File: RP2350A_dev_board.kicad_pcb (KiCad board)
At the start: 2 copper layers, 50 x 60 mm, 52 parts, among them J1 Debug Headers, J2 USB_C_Female_USB2.0_16P, J3 I2C Headers, SW1 Button, SW2 Bootstrap, U1 USBLC6-2SC6, U2 SPX3819M5-L-3-3, U3 RP2350A, U4 W25Q128JVS, Y2 12MHz Crystal GND2,4

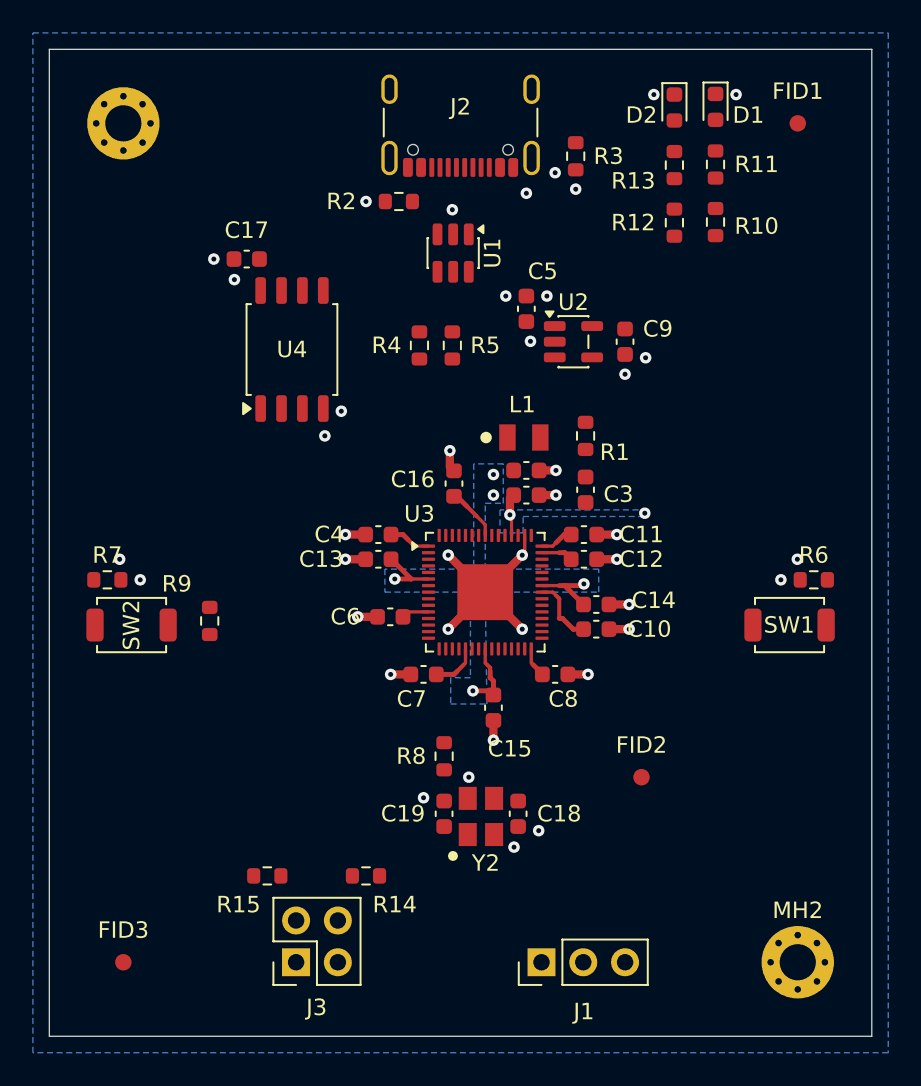
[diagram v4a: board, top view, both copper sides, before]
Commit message: Replaced +1V1 and +3V3 planes with wide routes. Routed all power. Finished all routing.
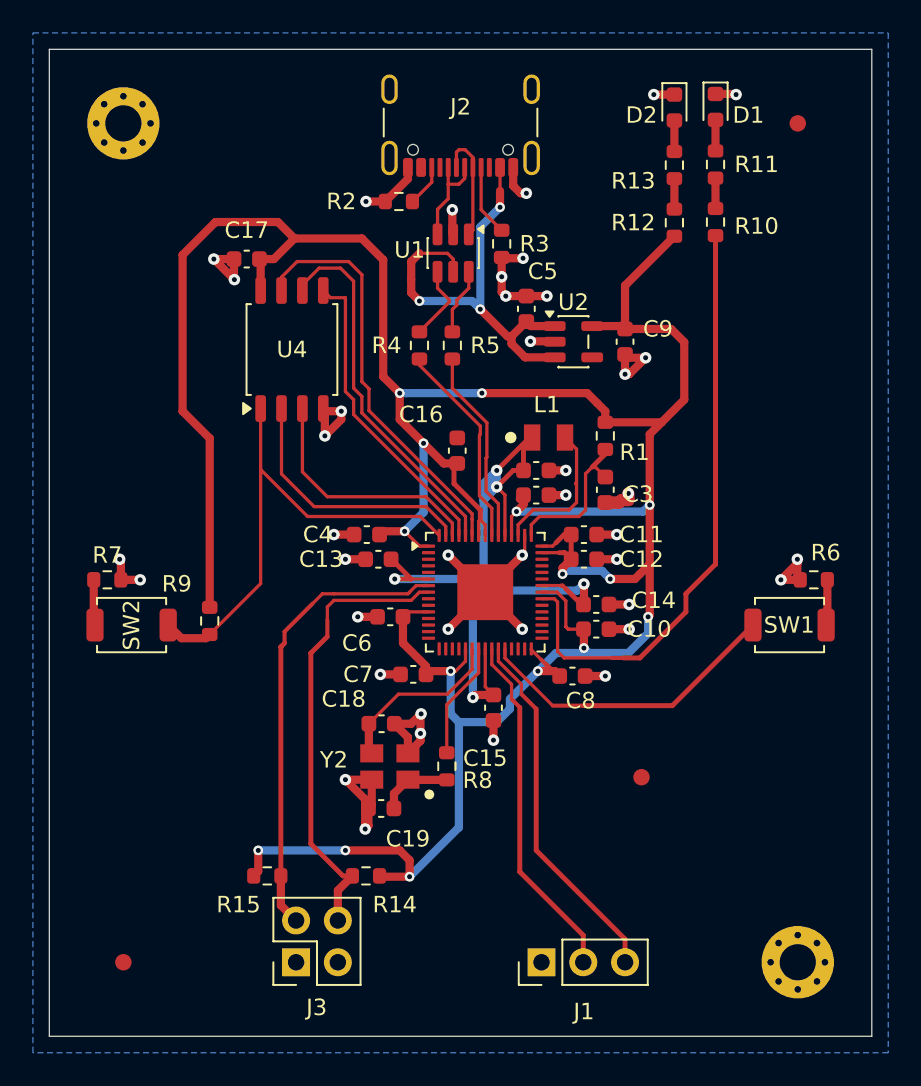
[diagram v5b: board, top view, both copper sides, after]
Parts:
- moved C18 9.94 mm to (143.2, 112.0), turned to 180 degrees
- moved R3 6.97 mm to (150.5, 82.8)
- moved Y2 4.99 mm to (145.5, 115.4), turned to 180 degrees
- moved C19 3.84 mm to (143.2, 117.2), turned to 0 degrees
- moved C16 2.01 mm to (147.8, 95.4)
- moved L1 1.50 mm to (154.3, 94.6)
- moved C3 1.20 mm to (156.8, 97.8)
- moved R1 1.20 mm to (156.8, 94.5)
- moved C8 1.05 mm to (154.8, 109.1)
- moved C4 0.70 mm to (142.3, 100.5)
- moved R8 0.63 mm to (147.2, 114.6)
- moved C7 0.62 mm to (145.1, 109.0)
- moved C1 0.60 mm to (152.6, 98.1)
- moved C2 0.60 mm to (152.6, 96.6)
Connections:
- net /USB_DM renamed /USB_DN
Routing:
- net +3V3: track 23.0 -> 204.5 mm, vias 2 -> 15
- net GND: track 29.6 -> 82.7 mm
- net +1V1: track 12.4 -> 52.8 mm
- net /GPIO25: track 0.00 -> 36.8 mm
- net /QSPI_SS: track 0.00 -> 30.5 mm
- net +VBUS: track 0.00 -> 28.4 mm, vias 0 -> 3
- net /I2C0_SDA: track 0.00 -> 27.9 mm
- net /I2C0_SCL: track 0.00 -> 27.7 mm
- net /QSPI_SD3: track 0.00 -> 25.0 mm
- net /QSPI_SCLK: track 0.00 -> 22.5 mm
- net /SWDIO: track 0.00 -> 22.2 mm
- net /SWCLK: track 0.00 -> 21.4 mm
- net Net-(U3-RUN): track 0.00 -> 18.9 mm
- net /QSPI_SD0: track 0.00 -> 18.8 mm
- net /QSPI_SD1: track 0.00 -> 15.8 mm
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- removed copper zone on B.Cu, net +1V1
- removed copper zone on B.Cu, net +3V3

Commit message: Finished routing. Cleared ERC on schematic and layout.
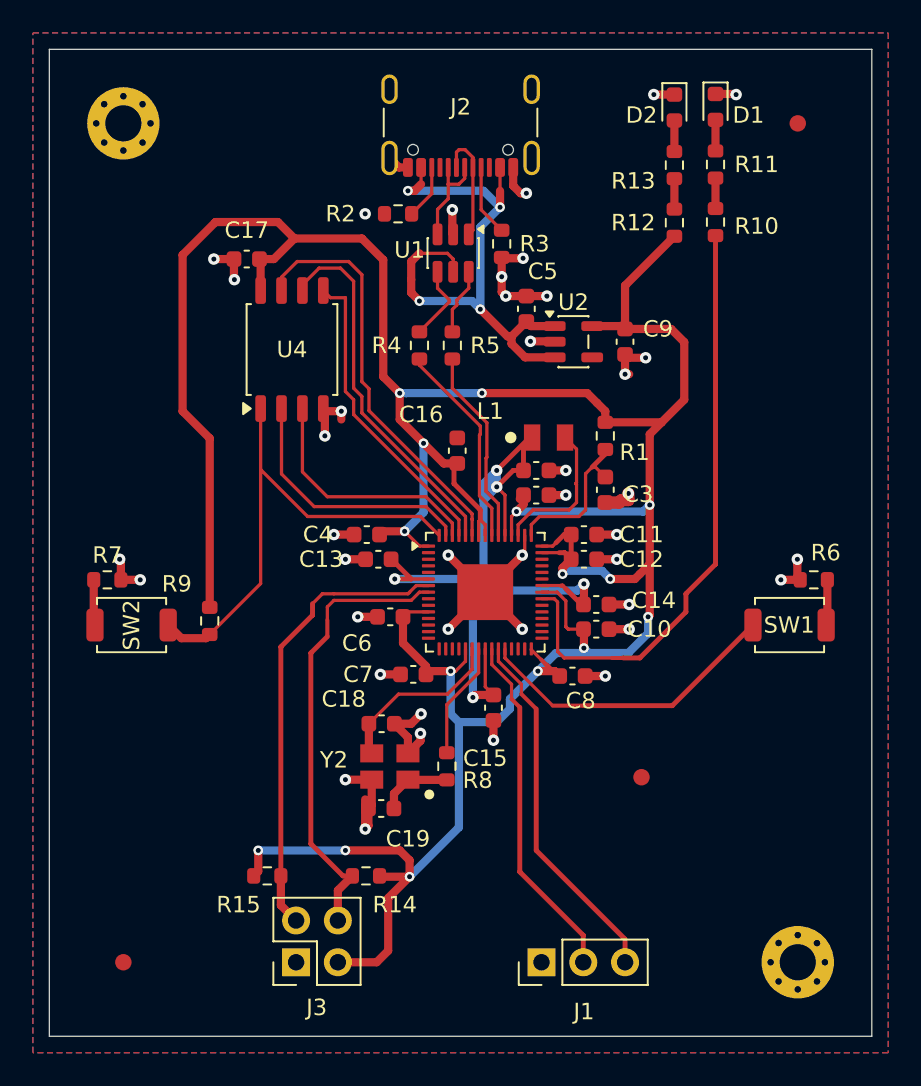
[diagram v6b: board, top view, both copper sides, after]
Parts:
- moved R2 0.75 mm to (144.2, 81.0)
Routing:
- net GND: track 82.7 -> 71.4 mm
- net +3V3: track 204.5 -> 212.9 mm
- net +VBUS: track 28.4 -> 36.4 mm, vias 3 -> 4
- net Net-(J2-CC2): track 2.56 -> 3.33 mm
- added copper zone on F.Cu, net GND
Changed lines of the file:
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@@
 		(at 154.35 94.6 180)
 		(property "Reference" "L1"
-			(at 1.1 2 0)
+			(at 4.55 1.6 0)
 			(unlocked yes)
 			(layer "F.SilkS")
@@
 			(pinfunction "GND")
 			(pintype "passive")
+			(zone_connect 2)
 		)
 		(pad "B1" smd roundrect
@@
 	(footprint "Resistor_SMD:R_0603_1608Metric"
 		(layer "F.Cu")
-		(at 144.25 80.25 180)
+		(at 144.2 81 180)
 		(descr "Resistor SMD 0603 (1608 Metric), square (rectangular) end terminal, IPC-7351 nominal, (Body size source: IPC-SM-782 page 72, https://www.pcb-3d.com/wordpress/wp-content/uploads/ipc-sm-782a_amendment_1_and_2.pdf), generated with kicad-footprint-generator")
 		(tags "resistor")
@@
 	)
 	(segment
+		(start 143.6 122.6)
+		(end 144.9 121.3)
+		(width 0.5)
+		(layer "F.Cu")
+		(net 1)
+	)
+	(segment
 		(start 154.2 102.9)
 		(end 154.2 102.525)
@@
 	)
 	(segment
+		(start 143.6 125.8)
+		(end 143.6 122.6)
+		(width 0.5)
+		(layer "F.Cu")
+		(net 1)
+	)
+	(segment
 		(start 155.475 106.25)
 		(end 154.55 106.25)
@@
 	)
 	(segment
+		(start 140.54 126.5)
+		(end 142.9 126.5)
+		(width 0.5)
+		(layer "F.Cu")
+		(net 1)
+	)
+	(segment
 		(start 145.9 109)
 		(end 145.9 108.5)
@@
 	)
 	(segment
+		(start 142.9 126.5)
+		(end 143.6 125.8)
+		(width 0.5)
+		(layer "F.Cu")
+		(net 1)
+	)
+	(segment
 		(start 147.6 97.4)
 		(end 147.6 96.375)
@@
 	)
 	(segment
-		(start 144.8 78.18)
-		(end 144.8 78.875)
-		(width 0.5)
-		(layer "F.Cu")
-		(net 2)
-	)
-	(segment
 		(start 147.5 82.2)
 		(end 147.55 82.25)
@@
 	)
 	(segment
-		(start 168.475 102.25)
-		(end 167.475 103.25)
-		(width 0.5)
-		(layer "F.Cu")
-		(net 2)
-	)
-	(segment
 		(start 154.4 98.1)
 		(end 153.375 98.1)
@@
 	)
 	(segment
-		(start 144.8 78.875)
-		(end 143.425 80.25)
-		(width 0.5)
-		(layer "F.Cu")
-		(net 2)
-	)
-	(segment
 		(start 151.65 79.75)
 		(end 151.2 79.3)
@@
 	)
 	(segment
-		(start 140.75 93.5)
-		(end 139.75 94.5)
+		(start 144.8 78.18)
+		(end 144.255 78.18)
 		(width 0.5)
 		(layer "F.Cu")
@@
 	)
 	(segment
-		(start 158.25 90.75)
-		(end 159.25 89.75)
-		(width 0.5)
-		(layer "F.Cu")
-		(net 2)
-	)
-	(segment
 		(start 168.475 103.075)
 		(end 168.65 103.25)
@@
 	)
 	(segment
-		(start 145.5625 112.5875)
-		(end 145.5625 111.4375)
-		(width 0.5)
-		(layer "F.Cu")
-		(net 2)
-	)
-	(segment
 		(start 158.25 106.25)
 		(end 157.025 106.25)
@@
 	)
 	(segment
-		(start 134.25 85)
-		(end 133 83.75)
-		(width 0.5)
-		(layer "F.Cu")
-		(net 2)
-	)
-	(segment
 		(start 157.5 100.5)
 		(end 156.275 100.5)
@@
 	)
 	(segment
-		(start 142.2 116.6)
-		(end 141 115.4)
-		(width 0.5)
-		(layer "F.Cu")
-		(net 2)
-	)
-	(segment
 		(start 144.8 113.8)
 		(end 144.8 112.825)
@@
 	)
 	(segment
-		(start 143.425 80.25)
-		(end 142.25 80.25)
-		(width 0.5)
-		(layer "F.Cu")
-		(net 2)
-	)
-	(segment
 		(start 158.25 104.75)
 		(end 157.025 104.75)
@@
 	)
 	(segment
+		(start 144.255 78.18)
+		(end 143.68 77.605)
+		(width 0.5)
+		(layer "F.Cu")
+		(net 2)
+	)
+	(segment
 		(start 147.5 80.75)
 		(end 147.5 82.2)
@@
 	)
 	(via
-		(at 142.25 80.25)
+		(at 142.2 81)
 		(size 0.7)
 		(drill 0.3)
@@
 	)
 	(segment
+		(start 145.6 79.2)
+		(end 145.2 79.6)
+		(width 0.5)
+		(layer "F.Cu")
+		(net 5)
+	)
+	(segment
 		(start 153.725 89.725)
 		(end 151.925 89.725)
@@
 	)
 	(segment
+		(start 145.2 79.6)
+		(end 144.8 79.6)
+		(width 0.5)
+		(layer "F.Cu")
+		(net 5)
+	)
+	(segment
 		(start 150.4 78.18)
 		(end 150.4 79.6)
@@
 	)
 	(segment
+		(start 145.6 78.18)
+		(end 145.6 79.2)
+		(width 0.2)
+		(layer "F.Cu")
+		(net 5)
+	)
+	(segment
 		(start 147.55 83.75)
 		(end 147.2 83.4)
@@
 	)
 	(via
+		(at 144.8 79.6)
+		(size 0.6)
+		(drill 0.3)
+		(layers "F.Cu" "B.Cu")
+		(net 5)
+	)
+	(via
 		(at 149.2 86.8)
 		(size 0.6)
@@
 	)
 	(segment
+		(start 149.4 79.6)
+		(end 150.4 80.6)
+		(width 0.5)
+		(layer "B.Cu")
+		(net 5)
+	)
+	(segment
+		(start 144.8 79.6)
+		(end 149.4 79.6)
+		(width 0.5)
+		(layer "B.Cu")
+		(net 5)
+	)
+	(segment
 		(start 148.7 107.45)
 		(end 148.7 108.7)
@@
 	)
 	(segment
-		(start 146.25 79.075)
-		(end 145.075 80.25)
+		(start 146.25 79.775)
+		(end 145.025 81)
 		(width 0.2)
 		(layer "F.Cu")
@@
 	(segment
 		(start 146.25 78.18)
-		(end 146.25 79.075)
+		(end 146.25 79.775)
 		(width 0.2)
 		(layer "F.Cu")
@@
 	)
 	(segment
+		(start 139 105.4)
+		(end 137.075 107.325)
+		(width 0.3)
+		(layer "F.Cu")
+		(net 19)
+	)
+	(segment
 		(start 144.9 104)
 		(end 144.8 104.1)
@@
 	)
 	(segment
-		(start 137.3 106.4)
-		(end 137.3 107.1)
-		(width 0.25)
-		(layer "F.Cu")
-		(net 19)
-	)
-	(segment
 		(start 139 104.7)
-		(end 137.3 106.4)
-		(width 0.25)
-		(layer "F.Cu")
-		(net 19)
-	)
-	(segment
-		(start 137.3 107.1)
-		(end 137.075 107.325)
+		(end 139 105.4)
 		(width 0.3)
 		(layer "F.Cu")
@@
 		(net 2)
 		(net_name "GND")
-		(layer "B.Cu")
-		(name "B.Cu.GND")
+		(layers "F.Cu" "B.Cu")
+		(name "Cu.GND")
 		(hatch edge 0.5)
 		(connect_pads
-			(clearance 0.3)
+			(clearance 0.4)
 		)
 		(min_thickness 0.2)
@@
 			)
 		)
+	)
+	(zone
+		(net 0)
+		(net_name "")
+		(layers "F.Cu" "B.Cu")
+		(name "inductor_fill_keepout")
+		(hatch edge 0.5)
+		(connect_pads
+			(clearance 0)
+		)
+		(min_thickness 0.25)
+		(filled_areas_thickness no)
+		(keepout
+			(tracks allowed)
+			(vias allowed)
+			(pads allowed)
+			(copperpour not_allowed)
+			(footprints allowed)
+		)
+		(placement
+			(enabled no)
+			(sheetname "/")
+		)
+		(fill
+			(thermal_gap 0.5)
+			(thermal_bridge_width 0.5)
+		)
+		(polygon
+			(pts
+				(xy 150.8 93.2) (xy 150.8 96) (xy 155.8 96) (xy 155.8 93.2)
+			)
+		)

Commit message: Final commit for time being, getting board printed and assembled was outside my price range. Unfortunately, oldering 0604 components is also outside my skill range. Project needs to be reorganized using through-hole components.
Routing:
- net GND: vias 41 -> 80
